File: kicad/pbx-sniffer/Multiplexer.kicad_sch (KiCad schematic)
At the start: 3 parts, among them U5 74HC138, U6 74HC138, U7 74HC138

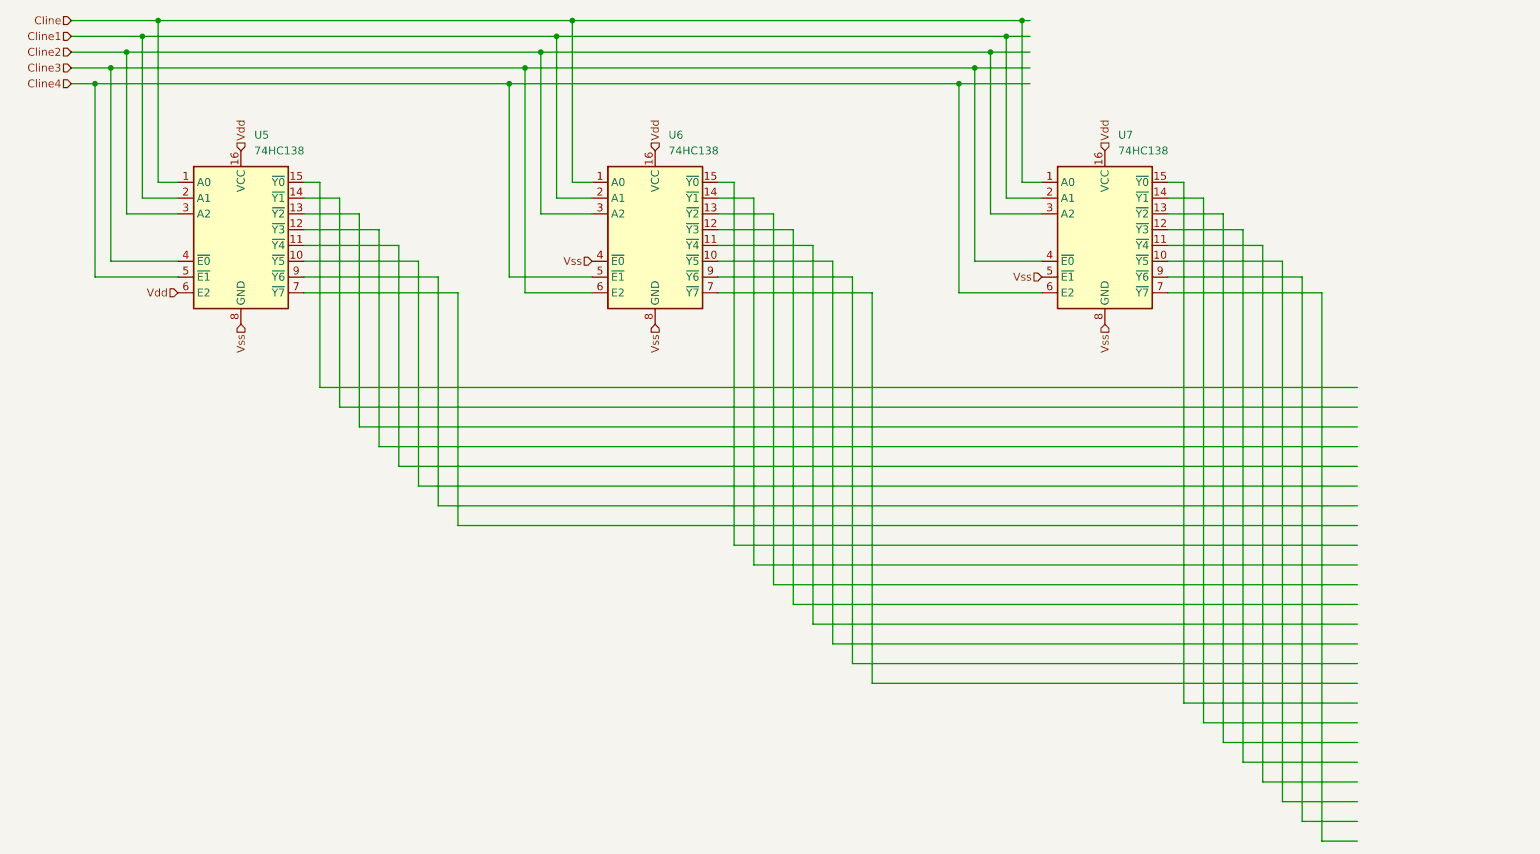
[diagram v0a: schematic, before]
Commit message: updated multiplexer with busses, added ADCs, fixed relay sch
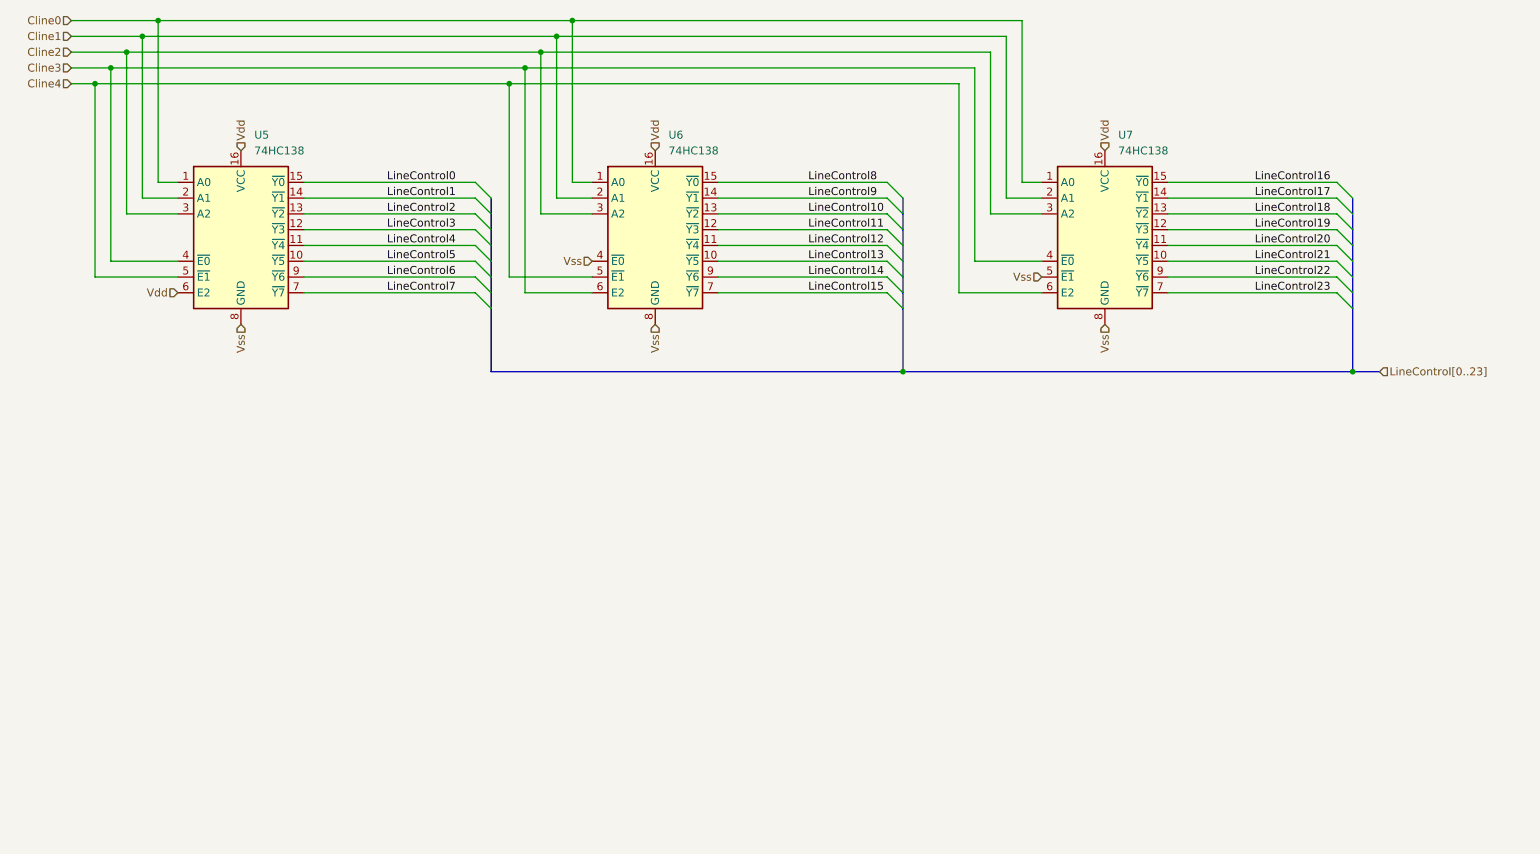
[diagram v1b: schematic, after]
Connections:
- net LineControl5: now reaches U5.10 (~{Y5})
- net LineControl4: now reaches U5.11 (~{Y4})
- net LineControl3: now reaches U5.12 (~{Y3})
- net LineControl2: now reaches U5.13 (~{Y2})
- net LineControl1: now reaches U5.14 (~{Y1})
- net LineControl0: now reaches U5.15 (~{Y0})
- net LineControl7: now reaches U5.7 (~{Y7})
- net LineControl6: now reaches U5.9 (~{Y6})
- net LineControl21: now reaches U7.10 (~{Y5})
- net LineControl20: now reaches U7.11 (~{Y4})
- net LineControl19: now reaches U7.12 (~{Y3})
- net LineControl18: now reaches U7.13 (~{Y2})
- net LineControl17: now reaches U7.14 (~{Y1})
- net LineControl16: now reaches U7.15 (~{Y0})
- net LineControl23: now reaches U7.7 (~{Y7})
- net LineControl22: now reaches U7.9 (~{Y6})
- net LineControl13: now reaches U6.10 (~{Y5})
- net LineControl12: now reaches U6.11 (~{Y4})
- net LineControl11: now reaches U6.12 (~{Y3})
- net LineControl10: now reaches U6.13 (~{Y2})
- net LineControl9: now reaches U6.14 (~{Y1})
- net LineControl8: now reaches U6.15 (~{Y0})
- net LineControl15: now reaches U6.7 (~{Y7})
- net LineControl14: now reaches U6.9 (~{Y6})
- net Cline renamed Cline0

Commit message: assigned footprints, added components to pcb
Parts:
- U5, U6, U7: footprint (none) -> Package_DIP:DIP-16_W7.62mm
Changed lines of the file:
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@@
 			)
 		)
-		(property "Footprint" ""
+		(property "Footprint" "Package_DIP:DIP-16_W7.62mm"
 			(at 59.055 62.23 0)
 			(effects
@@
 			)
 		)
-		(property "Footprint" ""
+		(property "Footprint" "Package_DIP:DIP-16_W7.62mm"
 			(at 198.12 62.23 0)
 			(effects
@@
 			)
 		)
-		(property "Footprint" ""
+		(property "Footprint" "Package_DIP:DIP-16_W7.62mm"
 			(at 125.73 62.23 0)
 			(effects

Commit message: commenced placement on pcb
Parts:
- renumbered U5 to U4, U6 to U5, U7 to U6
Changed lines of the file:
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@@
 		(dnp no)
 		(fields_autoplaced yes)
-		(property "Reference" "U5"
+		(property "Reference" "U4"
 			(at 61.1983 44.45 0)
 			(effects
@@
 			(project ""
 				(path "/4a5b9b8a-323a-4796-bf73-ccba532d2e31/e986fa27-3000-4fd4-977f-685db87b7fc5"
-					(reference "U5")
+					(reference "U4")
 					(unit 1)
 				)
@@
 		(dnp no)
 		(fields_autoplaced yes)
-		(property "Reference" "U7"
+		(property "Reference" "U6"
 			(at 200.2633 44.45 0)
 			(effects
@@
 			(project "pbx-sniffer"
 				(path "/4a5b9b8a-323a-4796-bf73-ccba532d2e31/e986fa27-3000-4fd4-977f-685db87b7fc5"
-					(reference "U7")
+					(reference "U6")
 					(unit 1)
 				)
@@
 		(dnp no)
 		(fields_autoplaced yes)
-		(property "Reference" "U6"
+		(property "Reference" "U5"
 			(at 127.8733 44.45 0)
 			(effects
@@
 			(project "pbx-sniffer"
 				(path "/4a5b9b8a-323a-4796-bf73-ccba532d2e31/e986fa27-3000-4fd4-977f-685db87b7fc5"
-					(reference "U6")
+					(reference "U5")
 					(unit 1)
 				)

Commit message: add part numbers for remaining important parts
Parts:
- U4, U5, U6: DKPN (none) -> 296-1575-5-ND
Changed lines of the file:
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@@
+			)
+		)
+		(property "DKPN" "296-1575-5-ND"
+			(at 59.055 62.23 0)
+			(effects
+				(font
+					(size 1.27 1.27)
+				)
+				(hide yes)
 			)
 		)
@@
 			)
 		)
+		(property "DKPN" "296-1575-5-ND"
+			(at 198.12 62.23 0)
+			(effects
+				(font
+					(size 1.27 1.27)
+				)
+				(hide yes)
+			)
+		)
 		(pin "5"
 		)
@@
 			(at 125.73 62.23 0)
 			(effects
+				(font
+					(size 1.27 1.27)
+				)
+				(hide yes)
+			)
+		)
+		(property "DKPN" "296-1575-5-ND"
+			(at 125.73 62.23 0)
+			(effects
